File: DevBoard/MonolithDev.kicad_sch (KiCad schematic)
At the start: 4 parts

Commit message: Dev board rev A8 part 2: review 4 docs, BOM, A-2 procedure, J104 clamp
Schematic edits by tools/review4_docs.py (helpers split out of
review4_fixes.py into tools/sch_edit.py; review4_fixes output unchanged).
- A-2: EV2400 work only with 3V3 up (J104) and U301 in reset; checklist,
  R312/R301 Notes and MCU sheet note 10 rewritten.
- D-5: D105 SMAJ18A clamp on the J104 side of D104; board placed
  (D104 moved one body width left).
- Stale Notes, sheet notes, heading and address text fixed; sheet 4
  renamed "MCU and Sensors"; revision log A7/A8; title blocks A8.
- MPNs filled on the parts that had only LCSC numbers; Sourcing on U301
  and J301; J301 out of the position file.
- bringup-config-checklist, mcu-io-power-states and power-budget rewritten
  for the CC2340 with every review 4 CONFIG item; corrections in
  circuit-description, cost-down and cc2340-pin-budget.
ERC: 8 known warnings. 0 text overlaps. DRC: 0 parity issues, no
courtyard overlaps (429 parts). README item 42.

Co-Authored-By: Claude Opus 5.5 <noreply@anthropic.com>
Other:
- sheet MCU and NTCs renamed MCU and Sensors
- note added: "MONOLITH DEV BOARD - SHEET INDEX 2. Cells and Gauge: 4S holders / pack input, BQ40Z50-R2 gauge, protection FETs, BQ294700 + F102 second-level protection, SMBus 3. Sleep Current and 3V3: R_MEAS + 2x INA190 to test loops, HT7550-1 amp supply, TPS62177 3V3 rail 4. MCU and Sensors: CC2340R5MODA, debug headers, TMP1075 board temperature sensors, status LED 5. USB Port 1 / 6. USB Port 2 (one sheet file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"
- note added: "TPS25751 ADDRESS / DEAD-BATTERY STRAPS (SafeMode) Port 1: R1 ADCIN1 = LDO_3V3, R2 ADCIN2 = GND -> I2C 0x20 Port 2: R3 ADCIN1 = GND, R4 ADCIN2 = GND -> I2C 0x21 Same SDA/SCL bus (CC2340 I2C0, 100 kHz): gauge BQ40Z50-R2 0x0B, TMP1075 U302-U306 0x48-0x4C"
- note removed: "MONOLITH DEV BOARD - SHEET INDEX 2. Cells and Gauge: 4S holders / pack input, BQ40Z50-R2 gauge, protection FETs, BQ294700 + F102 second-level protection, SMBus 3. Sleep Current and 3V3: R_MEAS + 2x INA190 to test loops, HT7550-1 amp supply, TPS62177 3V3 rail 4. MCU and NTCs: CC2340R5MODA, debug headers, TMP1075 board temperature sensors, status LED 5. USB Port 1 / 6. USB Port 2 (one sheet file): 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"
- note removed: "TPS25751 ADDRESS / DEAD-BATTERY STRAPS (SafeMode) Port 1: R1 ADCIN1 = LDO_3V3, R2 ADCIN2 = GND -> I2C 0x20 Port 2: R3 ADCIN1 = GND, R4 ADCIN2 = GND -> I2C 0x21 Gauge BQ40Z50-R2 = 0x0B on the same SDA/SCL bus (STM32WB I2C1, 100 kHz)"
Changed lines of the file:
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@@
 		(title "Monolith dev board - top level")
 		(date "2026-10-14")
-		(rev "A6")
+		(rev "A8")
 		(company "Monolith 100 W battery bank - dev board")
 		(comment 1 "Sheet index, PD address straps")
@@
 		(comment 3 "Reviewed 3x (docs/devboard); board placed, not routed or built")
 	)
-	(text "MONOLITH DEV BOARD - SHEET INDEX\n2.  Cells and Gauge:  4S holders / pack input, BQ40Z50-R2 gauge, protection FETs, BQ294700 + F102 second-level protection, SMBus\n3.  Sleep Current and 3V3:  R_MEAS + 2x INA190 to test loops, HT7550-1 amp supply, TPS62177 3V3 rail\n4.  MCU and NTCs:  CC2340R5MODA, debug headers, TMP1075 board temperature sensors, status LED\n5.  USB Port 1  /  6.  USB Port 2  (one sheet file):  TPS25751D + TPD4S201 + BQ25756 + TPS62933 per port\nRails (power symbols): PACK_P, 3V3, GND, CELL_N (gauge VSS only)\nSpec: docs/devboard/circuit-description.md.  Changes and open items: DevBoard/README.md"
+	(text "MONOLITH DEV BOARD - SHEET INDEX\n2.  Cells and Gauge:  4S holders / pack input, BQ40Z50-R2 gauge, protection FETs, BQ294700 + F102 second-level protection, SMBus\n3.  Sleep Current and 3V3:  R_MEAS + 2x INA190 to test loops, HT7550-1 amp supply, TPS62177 3V3 rail\n4.  MCU and Sensors:  CC2340R5MODA, debug headers, TMP1075 board temperature sensors, status LED\n5.  USB Port 1  /  6.  USB Port 2  (one sheet file):  TPS25751D + TPD4S201 + BQ25756 + TPS62933 per port\nRails (power symbols): PACK_P, 3V3, GND, CELL_N (gauge VSS only)\nSpec: docs/devboard/circuit-description.md.  Changes and open items: DevBoard/README.md"
 		(exclude_from_sim no)
 		(at 30.48 205.74 0)
@@
 		)
 	)
-	(text "REVISION LOG\nA0  2026-10-11  First draft from circuit description draft 5.  Author: Claude Code.  Reviewer: none yet.\nA1  2026-10-11  Layout cleanup: blocks, power symbols, notes, title blocks.  Author: Claude Code.  Reviewer: none yet.\nA2  2026-10-11  Readability pass: no overlapping text, sheet-pin names inside boxes.  Author: Claude Code.  Reviewer: none yet.\nA3  2026-10-11  Wiring pass: wires instead of labels inside each block.  Author: Claude Code.  Reviewer: none yet.\nA4  2026-10-12  Polymer bulk caps, PWR_FLAGs at rail sources, design-review fixes\n                (docs/devboard/schematic-review-2026-10-12.md).  Author: Claude Code.  Reviewer: 3-agent review.\nA5  2026-10-13  Review 2 decisions: CHG_INH fails safe (R417/R517 47k pull-up to 3V3, MCU drives low to charge),\n                MCU IWDG in hardware mode; BAT fed before F101 (TI fig. 9-12); C421/C521 100 uF; LRB520S, BSS138,\n                C109 4.7n, PPHV/VBUS caps, GND/probe test points, JLC numbers on all R/C (review 2);\n                J201/J202 SMAs replaced by OUT_LO/OUT_HI loops TP201/TP202 + GND loops TP208/TP209.  Author: Claude Code.\nA6  2026-10-14  Branch hand-review: second-level protection U102 BQ294700 + F102 WSFB1514 (TI fig. 9-11), F101 deleted;\n                D103 fitted; U202 INA190A1 JLC-placed; R405-R408 removed; USB-C liquid detection (U405/U505 TPD2S300,\n                Q403-Q406, R440/R540 DCP short, D403/D503 removed). Review 3: TPD2S300 FLT -> GPIO3 (R441), liquid-detect\n                gate pulls R442/R443, BQ25756 gate/BTST 0R R444-R449 + DNP snubbers, U401 symbol GPIO11 bidirectional.\n                Cost-down (docs/devboard/cost-down-2026-10-14.md): L401/L501 SMMS1040, L402/L502 APS0530, L201 FNR4030S,\n                U203 HT7550-1, 22u 1206 battery bank, basic/preferred passives, Q103 AO3400A, D301 red, R431 solder\n                jumper, 34 test loops -> pads, headers hand-soldered, U301 consigned.\n                Charger half-bridges IAUC45N04 -> 4 discrete PGQ04N070 per port (Q401/Q402 + new Q407/Q408).\n                6-layer 1.6 mm board (0.3 mm vias): U405/U505 TPD2S300 -> TPD4S201 (CC + SBU), D402/D502 removed,\n                J401/J501 -> TYPE-C 16PCB1.6 IP68.\n                Board: block placement (tools/place_blocks.py). Schematic tidy: title blocks, headings, MCU notes and test points.\n                Author: Logan (hand review) + Claude Code."
-		(exclude_from_sim no)
-		(at 30.48 260.35 0)
-		(effects
-			(font
-				(size 1.27 1.27)
-			)
-			(justify left bottom)
-		)
-	)
-	(text "TPS25751 ADDRESS / DEAD-BATTERY STRAPS (SafeMode)\nPort 1: R1 ADCIN1 = LDO_3V3, R2 ADCIN2 = GND  -> I2C 0x20\nPort 2: R3 ADCIN1 = GND,     R4 ADCIN2 = GND  -> I2C 0x21\nGauge BQ40Z50-R2 = 0x0B on the same SDA/SCL bus (STM32WB I2C1, 100 kHz)"
+	(text "REVISION LOG\nA0  2026-10-11  First draft from circuit description draft 5.  Author: Claude Code.  Reviewer: none yet.\nA1  2026-10-11  Layout cleanup: blocks, power symbols, notes, title blocks.  Author: Claude Code.  Reviewer: none yet.\nA2  2026-10-11  Readability pass: no overlapping text, sheet-pin names inside boxes.  Author: Claude Code.  Reviewer: none yet.\nA3  2026-10-11  Wiring pass: wires instead of labels inside each block.  Author: Claude Code.  Reviewer: none yet.\nA4  2026-10-12  Polymer bulk caps, PWR_FLAGs at rail sources, design-review fixes\n                (docs/devboard/schematic-review-2026-10-12.md).  Author: Claude Code.  Reviewer: 3-agent review.\nA5  2026-10-13  Review 2 decisions: CHG_INH fails safe (R417/R517 47k pull-up to 3V3, MCU drives low to charge),\n                MCU IWDG in hardware mode; BAT fed before F101 (TI fig. 9-12); C421/C521 100 uF; LRB520S, BSS138,\n                C109 4.7n, PPHV/VBUS caps, GND/probe test points, JLC numbers on all R/C (review 2);\n                J201/J202 SMAs replaced by OUT_LO/OUT_HI loops TP201/TP202 + GND loops TP208/TP209.  Author: Claude Code.\nA6  2026-10-14  Branch hand-review: second-level protection U102 BQ294700 + F102 WSFB1514 (TI fig. 9-11), F101 deleted;\n                D103 fitted; U202 INA190A1 JLC-placed; R405-R408 removed; USB-C liquid detection (U405/U505 TPD2S300,\n                Q403-Q406, R440/R540 DCP short, D403/D503 removed). Review 3: TPD2S300 FLT -> GPIO3 (R441), liquid-detect\n                gate pulls R442/R443, BQ25756 gate/BTST 0R R444-R449 + DNP snubbers, U401 symbol GPIO11 bidirectional.\n                Cost-down (docs/devboard/cost-down-2026-10-14.md): L401/L501 SMMS1040, L402/L502 APS0530, L201 FNR4030S,\n                U203 HT7550-1, 22u 1206 battery bank, basic/preferred passives, Q103 AO3400A, D301 red, R431 solder\n                jumper, 34 test loops -> pads, headers hand-soldered, U301 consigned.\n                Charger half-bridges IAUC45N04 -> 4 discrete PGQ04N070 per port (Q401/Q402 + new Q407/Q408).\n                6-layer 1.6 mm board (0.3 mm vias): U405/U505 TPD2S300 -> TPD4S201 (CC + SBU), D402/D502 removed,\n                J401/J501 -> TYPE-C 16PCB1.6 IP68.\n                Board: block placement (tools/place_blocks.py). Schematic tidy: title blocks, headings, MCU notes and test points.\n                Author: Logan (hand review) + Claude Code.\nA7  2026-10-14  U301 STM32WB1MMC -> CC2340R5MODA with RF match C313-C315/R321; TMP1075 U302-U306 (U305/U306 DNP)\n                replace TH301-TH305, NTC_EN and their dividers; IRQ1/IRQ2/GAUGE_BTP -> one open-drain IRQ_N\n                (R314 pull-up, R315/R114 DNP); R313 fitted; TMP1075 footprint with 0.3 mm vias.  Author: Claude Code.\nA8  2026-10-14  Review 4 (docs/devboard/schematic-review-4-2026-10-14.md): R313 220k, R314 47k, R304/R305 3.3k,\n                R322-R324 series resistors at J302/J303, C401/C402 220p, D401/D501 TVS2200, snubber R 1206,\n                TP415-TP421 probe pads, D105 J104 clamp; Notes, sheet text and MPNs updated; sheet 4 renamed\n                MCU and Sensors.  Author: Claude Code.  Reviewer: 4-agent review + Logan."
+		(exclude_from_sim no)
+		(at 30.48 265.43 0)
+		(effects
+			(font
+				(size 1.27 1.27)
+			)
+			(justify left bottom)
+		)
+	)
+	(text "TPS25751 ADDRESS / DEAD-BATTERY STRAPS (SafeMode)\nPort 1: R1 ADCIN1 = LDO_3V3, R2 ADCIN2 = GND  -> I2C 0x20\nPort 2: R3 ADCIN1 = GND,     R4 ADCIN2 = GND  -> I2C 0x21\nSame SDA/SCL bus (CC2340 I2C0, 100 kHz): gauge BQ40Z50-R2 0x0B, TMP1075 U302-U306 0x48-0x4C"
 		(exclude_from_sim no)
 		(at 106.68 184.15 0)
@@
 			(color 0 0 0 0)
 		)
-		(property "Sheetname" "MCU and NTCs"
+		(property "Sheetname" "MCU and Sensors"
 			(at 172.54 38.73 0)
 			(show_name no)

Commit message: Dev board: downsize passives to 0402 where basic parts allow
160 resistors and capacitors move to the smallest package that keeps their
rating: never below 0402, and no JLC basic part becomes extended. Connectivity
and ERC are unchanged, extended parts stay at 27, and the cost goes from
$108.49 to $107.93 per board at 2 boards. Applied by
tools/downsize_passives.py (one-shot); README item 45 lists what moved, what
stayed and why. The PCB still needs Update PCB from Schematic.

Co-Authored-By: Claude Opus 5.5 <noreply@anthropic.com>
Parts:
- R1, R2, R3, R4: footprint Resistor_SMD:R_0603_1608Metric -> Resistor_SMD:R_0402_1005Metric; LCSC C21189 -> C17168; MPN 0603WAF0000T5E -> 0402WGF0000TCE
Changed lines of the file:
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@@
 			)
 		)
-		(property "Footprint" "Resistor_SMD:R_0603_1608Metric"
+		(property "Footprint" "Resistor_SMD:R_0402_1005Metric"
 			(at 115.062 160.02 90)
 			(hide yes)
@@
 			)
 		)
-		(property "LCSC" "C21189"
+		(property "LCSC" "C17168"
 			(at 116.84 160.02 0)
 			(hide yes)
@@
 			)
 		)
-		(property "MPN" "0603WAF0000T5E"
+		(property "MPN" "0402WGF0000TCE"
 			(at 116.84 160.02 0)
 			(hide yes)
@@
 			)
 		)
-		(property "Footprint" "Resistor_SMD:R_0603_1608Metric"
+		(property "Footprint" "Resistor_SMD:R_0402_1005Metric"
 			(at 252.222 160.02 90)
 			(hide yes)
@@
 			)
 		)
-		(property "LCSC" "C21189"
+		(property "LCSC" "C17168"
 			(at 254 160.02 0)
 			(hide yes)
@@
 			)
 		)
-		(property "MPN" "0603WAF0000T5E"
+		(property "MPN" "0402WGF0000TCE"
 			(at 254 160.02 0)
 			(hide yes)
@@
 			)
 		)
-		(property "Footprint" "Resistor_SMD:R_0603_1608Metric"
+		(property "Footprint" "Resistor_SMD:R_0402_1005Metric"
 			(at 127.762 160.02 90)
 			(hide yes)
@@
 			)
 		)
-		(property "LCSC" "C21189"
+		(property "LCSC" "C17168"
 			(at 129.54 160.02 0)
 			(hide yes)
@@
 			)
 		)
-		(property "MPN" "0603WAF0000T5E"
+		(property "MPN" "0402WGF0000TCE"
 			(at 129.54 160.02 0)
 			(hide yes)
@@
 			)
 		)
-		(property "Footprint" "Resistor_SMD:R_0603_1608Metric"
+		(property "Footprint" "Resistor_SMD:R_0402_1005Metric"
 			(at 239.522 160.02 90)
 			(hide yes)
@@
 			)
 		)
-		(property "LCSC" "C21189"
+		(property "LCSC" "C17168"
 			(at 241.3 160.02 0)
 			(hide yes)
@@
 			)
 		)
-		(property "MPN" "0603WAF0000T5E"
+		(property "MPN" "0402WGF0000TCE"
 			(at 241.3 160.02 0)
 			(hide yes)

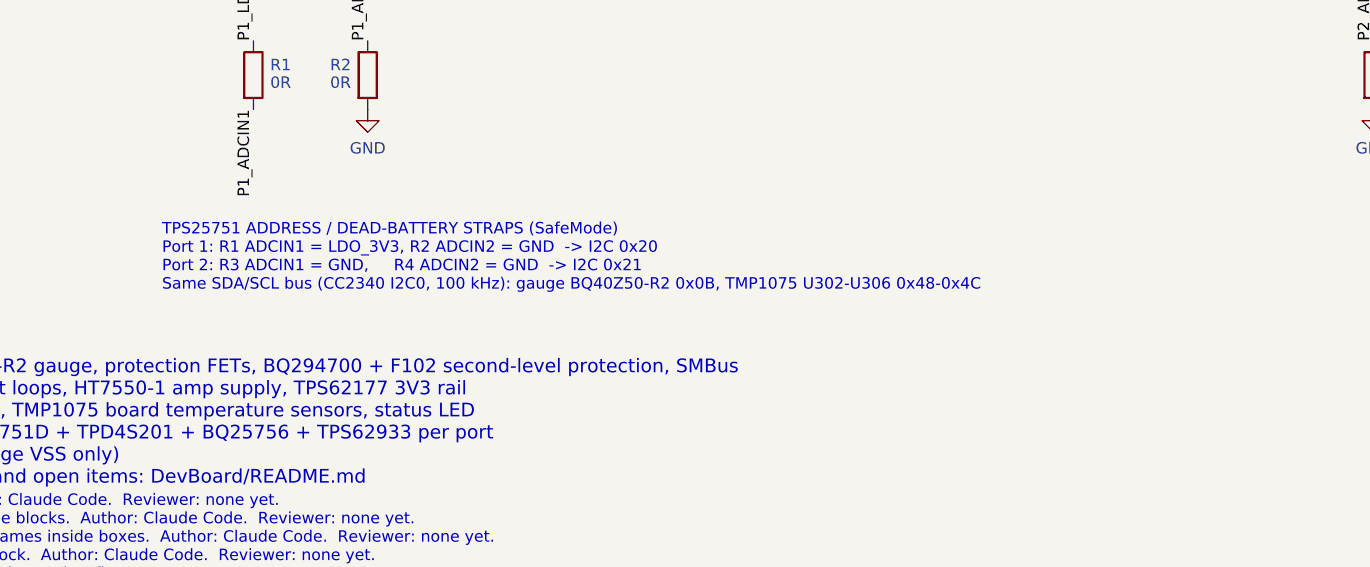
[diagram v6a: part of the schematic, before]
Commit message: Dev board: 10R gate resistors with turn-off diodes; remove TMP1075 sensors
Gate drive (both ports): R444-R447 / R544-R547 0R -> 10R, with a BAT54WS
(D406-D409 / D506-D509) across each, cathode at the BQ25756 driver pin, so
turn-off bypasses the resistor and the 45 ns dead time is kept. Notes on the
gate resistors rewritten (they named the wrong drivers). Diodes are staged
below the board for hand placement.

Board temperature (rev A8): U302-U306 and C308-C312 removed. Temperatures
now come from the gauge (DAStatus2: TS1-TS4, cell, FET, die; readable
sealed) and from each BQ25756 TS NTC via the TPS25751 'I2Cr' pass-through
(REG0x37 TS_ADC). IRQ_N now has three sources. Docs, power budget and
scripts updated.

Also includes the author's own uncommitted schematic and README edits.
ERC: 8 known warnings; DRC schematic parity: 0 footprint errors.

Co-Authored-By: Claude Opus 5.5 <noreply@anthropic.com>
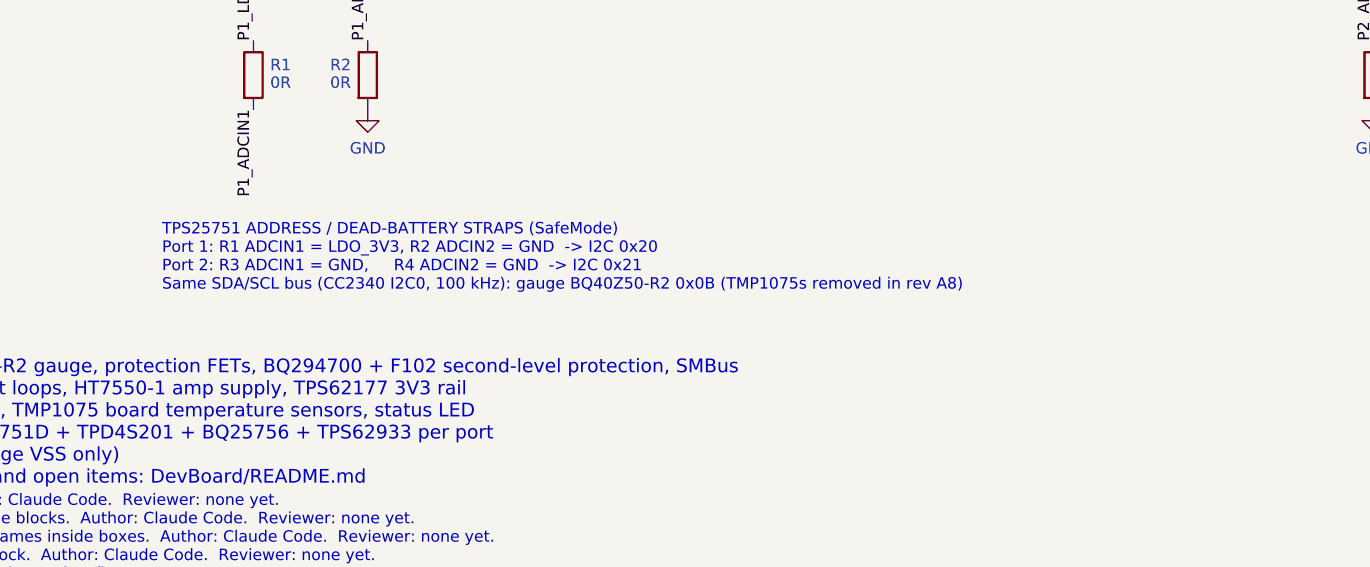
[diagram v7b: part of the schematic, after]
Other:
- note added: "TPS25751 ADDRESS / DEAD-BATTERY STRAPS (SafeMode) Port 1: R1 ADCIN1 = LDO_3V3, R2 ADCIN2 = GND -> I2C 0x20 Port 2: R3 ADCIN1 = GND, R4 ADCIN2 = GND -> I2C 0x21 Same SDA/SCL bus (CC2340 I2C0, 100 kHz): gauge BQ40Z50-R2 0x0B (TMP1075s removed in rev A8)"
- note removed: "TPS25751 ADDRESS / DEAD-BATTERY STRAPS (SafeMode) Port 1: R1 ADCIN1 = LDO_3V3, R2 ADCIN2 = GND -> I2C 0x20 Port 2: R3 ADCIN1 = GND, R4 ADCIN2 = GND -> I2C 0x21 Same SDA/SCL bus (CC2340 I2C0, 100 kHz): gauge BQ40Z50-R2 0x0B, TMP1075 U302-U306 0x48-0x4C"
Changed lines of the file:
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@@
 		)
 	)
-	(text "TPS25751 ADDRESS / DEAD-BATTERY STRAPS (SafeMode)\nPort 1: R1 ADCIN1 = LDO_3V3, R2 ADCIN2 = GND  -> I2C 0x20\nPort 2: R3 ADCIN1 = GND,     R4 ADCIN2 = GND  -> I2C 0x21\nSame SDA/SCL bus (CC2340 I2C0, 100 kHz): gauge BQ40Z50-R2 0x0B, TMP1075 U302-U306 0x48-0x4C"
+	(text "TPS25751 ADDRESS / DEAD-BATTERY STRAPS (SafeMode)\nPort 1: R1 ADCIN1 = LDO_3V3, R2 ADCIN2 = GND  -> I2C 0x20\nPort 2: R3 ADCIN1 = GND,     R4 ADCIN2 = GND  -> I2C 0x21\nSame SDA/SCL bus (CC2340 I2C0, 100 kHz): gauge BQ40Z50-R2 0x0B (TMP1075s removed in rev A8)"
 		(exclude_from_sim no)
 		(at 106.68 184.15 0)
